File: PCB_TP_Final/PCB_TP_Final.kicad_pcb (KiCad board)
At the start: 2 copper layers, 5 parts, among them CN10 Conn_02x17_Odd_Even, CN7 Conn_02x10_Odd_Even, CN8 Conn_02x08_Odd_Even, CN9 Conn_02x15_Odd_Even, J1 Conn_01x09

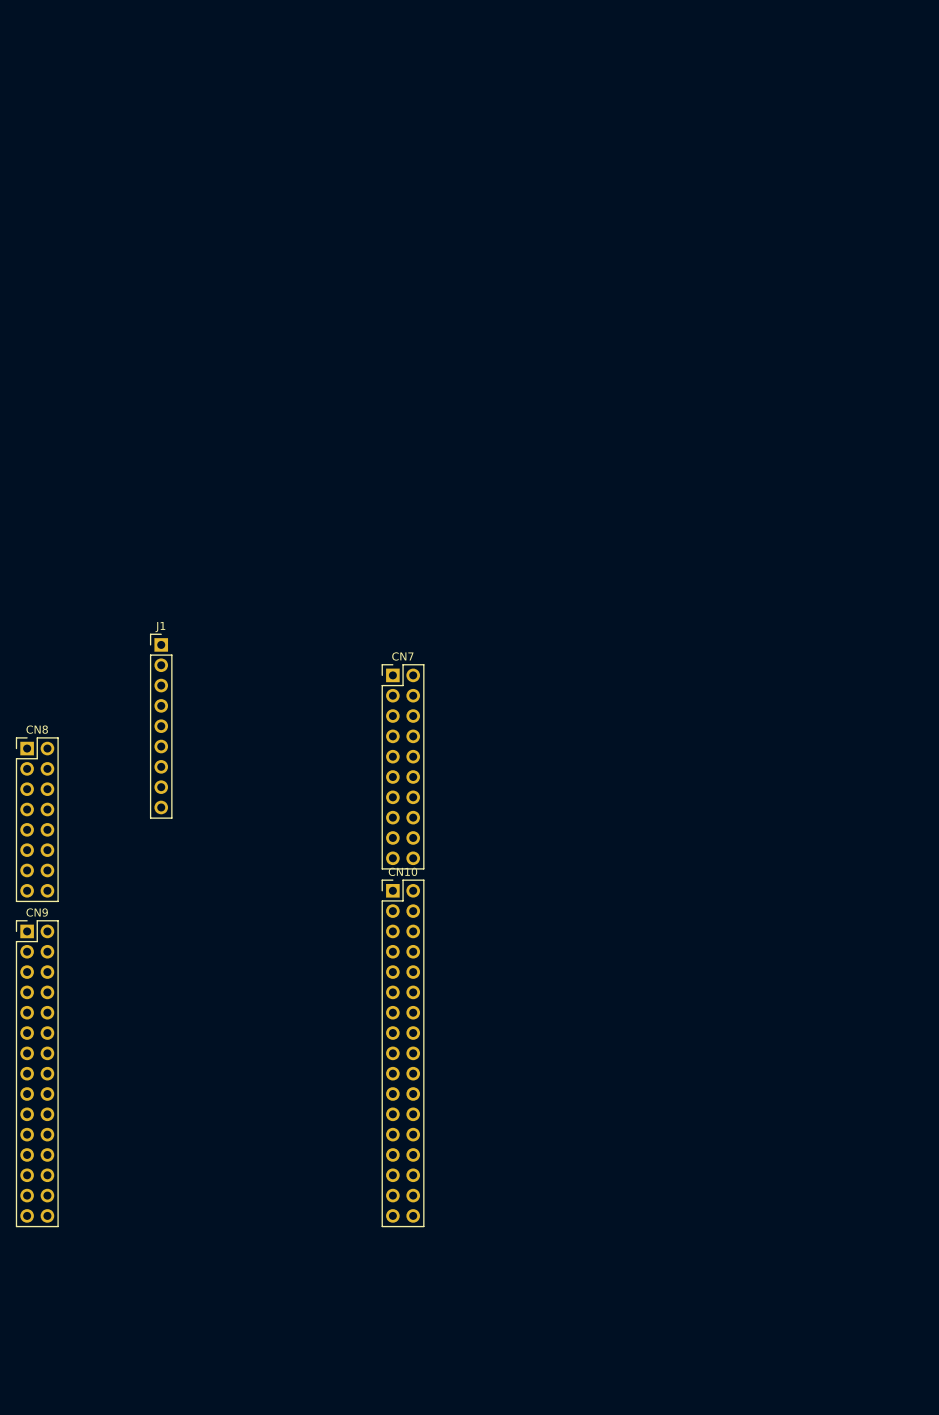
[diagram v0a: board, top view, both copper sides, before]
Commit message: Add footprint CODEC_AUDIO_WM8731
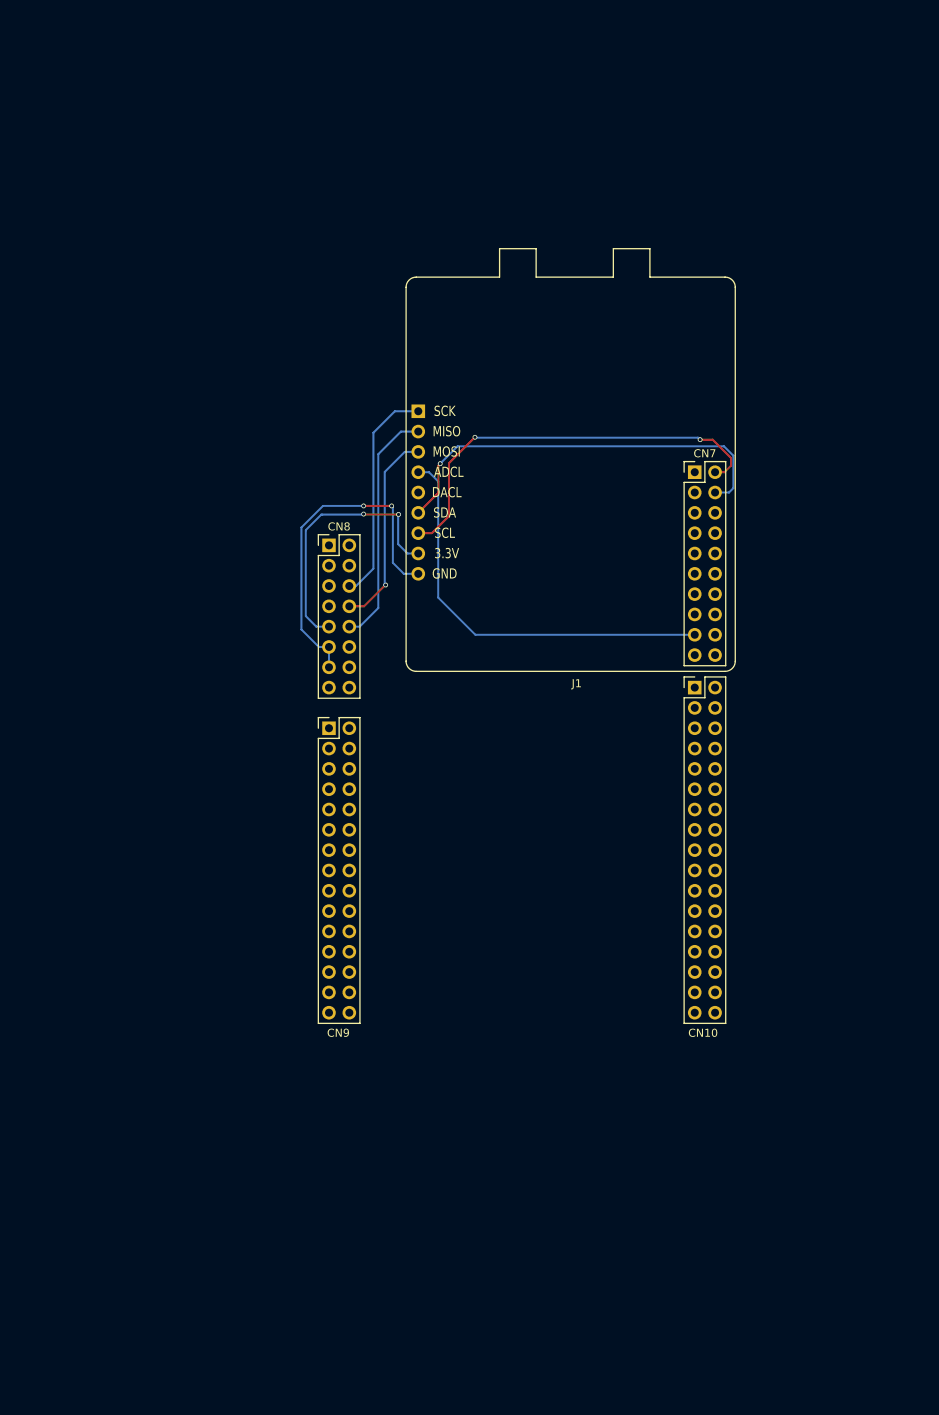
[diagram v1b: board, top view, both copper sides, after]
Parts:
- J1: footprint Connector_PinHeader_2.54mm:PinHeader_1x09_P2.54mm_Vertical -> CUSTOM_LIB:Audio_Codec_WM8731
- moved J1 55.0 mm to (132.2, 78.2)
- moved CN10 45.5 mm to (147.0, 101.6)
- moved CN8 45.5 mm to (101.2, 83.8)
- moved CN9 45.5 mm to (101.2, 106.7)
- moved CN7 45.5 mm to (147.0, 74.7)
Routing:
- net /AUDIO_CODEC/SCL: track 0.00 -> 52.3 mm, vias 0 -> 2
- net /AUDIO_CODEC/SDA: track 0.00 -> 51.9 mm, vias 0 -> 1
- net /AUDIO_CODEC/ADCL: track 0.00 -> 51.5 mm
- net GND: track 0.00 -> 43.0 mm, vias 0 -> 2
- net +3V3: track 0.00 -> 33.4 mm, vias 0 -> 2
- net /AUDIO_CODEC/MISO: track 0.00 -> 30.0 mm
- net /AUDIO_CODEC/SCK: track 0.00 -> 27.6 mm
- net /AUDIO_CODEC/MOSI: track 0.00 -> 25.1 mm, vias 0 -> 1

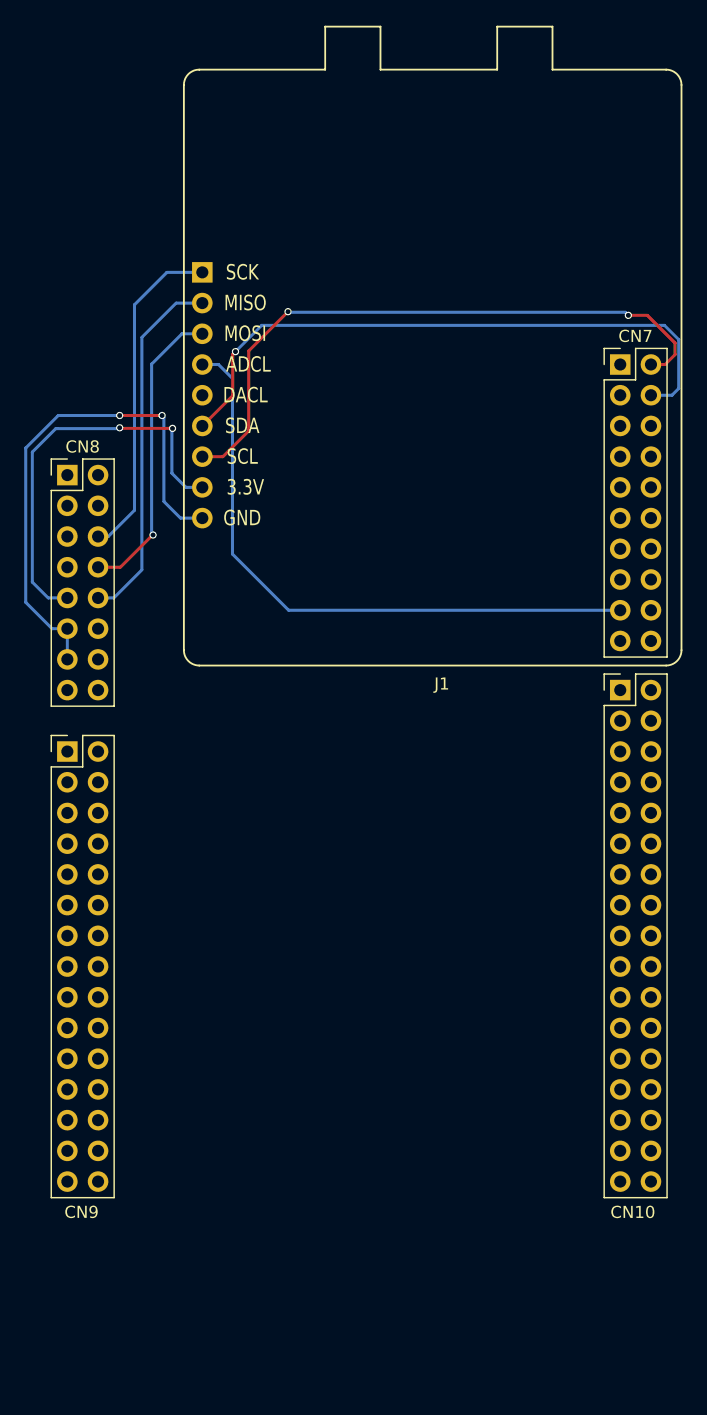
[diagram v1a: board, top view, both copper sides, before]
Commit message: Add 3D conections and NODEMCU ESP12
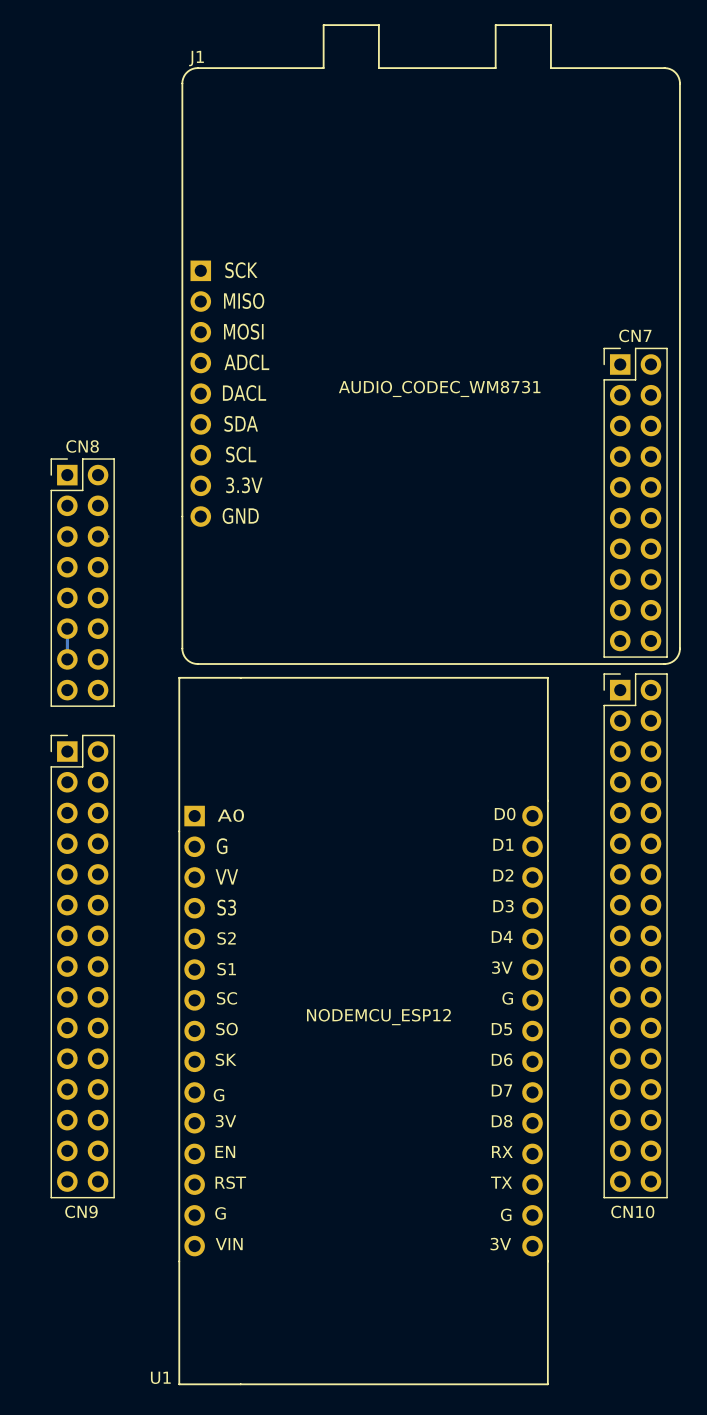
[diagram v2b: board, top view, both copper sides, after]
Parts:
- added U1: NODEMCU_ESP12, NODEMCU_ESP12:NODEMCU_ESP12, F.Cu at (127.0, 129.8)
- J1: footprint CUSTOM_LIB:Audio_Codec_WM8731 -> AUDIO_CODEC_WM8731:Audio_Codec_WM8731
- moved J1 0.18 mm to (132.1, 78.1)
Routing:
- net /AUDIO_CODEC/SCL: track 52.3 -> 0.00 mm, vias 2 -> 0
- net /AUDIO_CODEC/SDA: track 51.9 -> 0.00 mm, vias 1 -> 0
- net /AUDIO_CODEC/ADCL: track 51.5 -> 0.00 mm
- net GND: track 43.0 -> 2.54 mm, vias 2 -> 0
- net +3V3: track 33.4 -> 0.00 mm, vias 2 -> 0
- net /AUDIO_CODEC/MISO: track 30.0 -> 0.00 mm
- net /AUDIO_CODEC/SCK: track 27.6 -> 0.84 mm
- net /AUDIO_CODEC/MOSI: track 25.1 -> 0.00 mm, vias 1 -> 0

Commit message: Primera entrega (1.0) para revision
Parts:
- added M1: POWER_MB_V2, POWER_MB_V2:POWER_MB_V2, F.Cu at (124.5, 167.6)
- added R1: 3.3K, Resistors_SMD:R_1206, F.Cu at (120.0, 83.8)
- moved U1 2.29 mm to (127.0, 132.1)
- moved J1 0.90 mm to (131.4, 78.7)
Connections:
- CN10 pad 10: Net-(CN10-Pad10) -> /NODEMCU_ESP12/HMISO
- CN10 pad 26: Net-(CN10-Pad26) -> /NODEMCU_ESP12/HSCLK
- CN10 pad 28: Net-(CN10-Pad28) -> /NODEMCU_ESP12/HMOSI
- CN10 pad 6: Net-(CN10-Pad6) -> /NODEMCU_ESP12/HCS
- CN8 pad 9: +3V3 -> 3.3VB
- CN9 pad 12: Net-(CN9-Pad12) -> GND
- J1 pad 8: +3V3 -> 3.3VB
- U1 pad 16: Net-(U1-Pad16) -> +3V3
- U1 pad 20: Net-(U1-Pad20) -> /NODEMCU_ESP12/HCS
- U1 pad 21: Net-(U1-Pad21) -> /NODEMCU_ESP12/HMOSI
- U1 pad 22: Net-(U1-Pad22) -> /NODEMCU_ESP12/HMISO
- U1 pad 23: Net-(U1-Pad23) -> /NODEMCU_ESP12/HSCLK
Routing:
- net GND: track 2.54 -> 202.2 mm
- net /NODEMCU_ESP12/HMISO: track 0.00 -> 97.8 mm, vias 0 -> 1
- net /NODEMCU_ESP12/HCS: track 0.00 -> 93.5 mm, vias 0 -> 2
- net 3.3VB: track 0.00 -> 85.9 mm, vias 0 -> 1
- net /AUDIO_CODEC/SDA: track 0.00 -> 72.5 mm, vias 0 -> 2
- net /AUDIO_CODEC/ADCL: track 0.00 -> 51.3 mm
- net /AUDIO_CODEC/SCL: track 0.00 -> 49.5 mm, vias 0 -> 1
- net +3V3: track 0.00 -> 44.2 mm
- net /NODEMCU_ESP12/HSCLK: track 0.00 -> 40.6 mm
- net /AUDIO_CODEC/MOSI: track 0.00 -> 40.2 mm
- net /NODEMCU_ESP12/HMOSI: track 0.00 -> 32.9 mm
- net /AUDIO_CODEC/MISO: track 0.00 -> 28.8 mm, vias 0 -> 2
- net /AUDIO_CODEC/SCK: track 0.84 -> 27.9 mm
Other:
- board outline added: 61 x 127 mm
- net class Default: clearance 0.2 -> 0.4; trace_width 0.25 -> 0.6
- rule trace_clearance: 0.2 -> 0.4

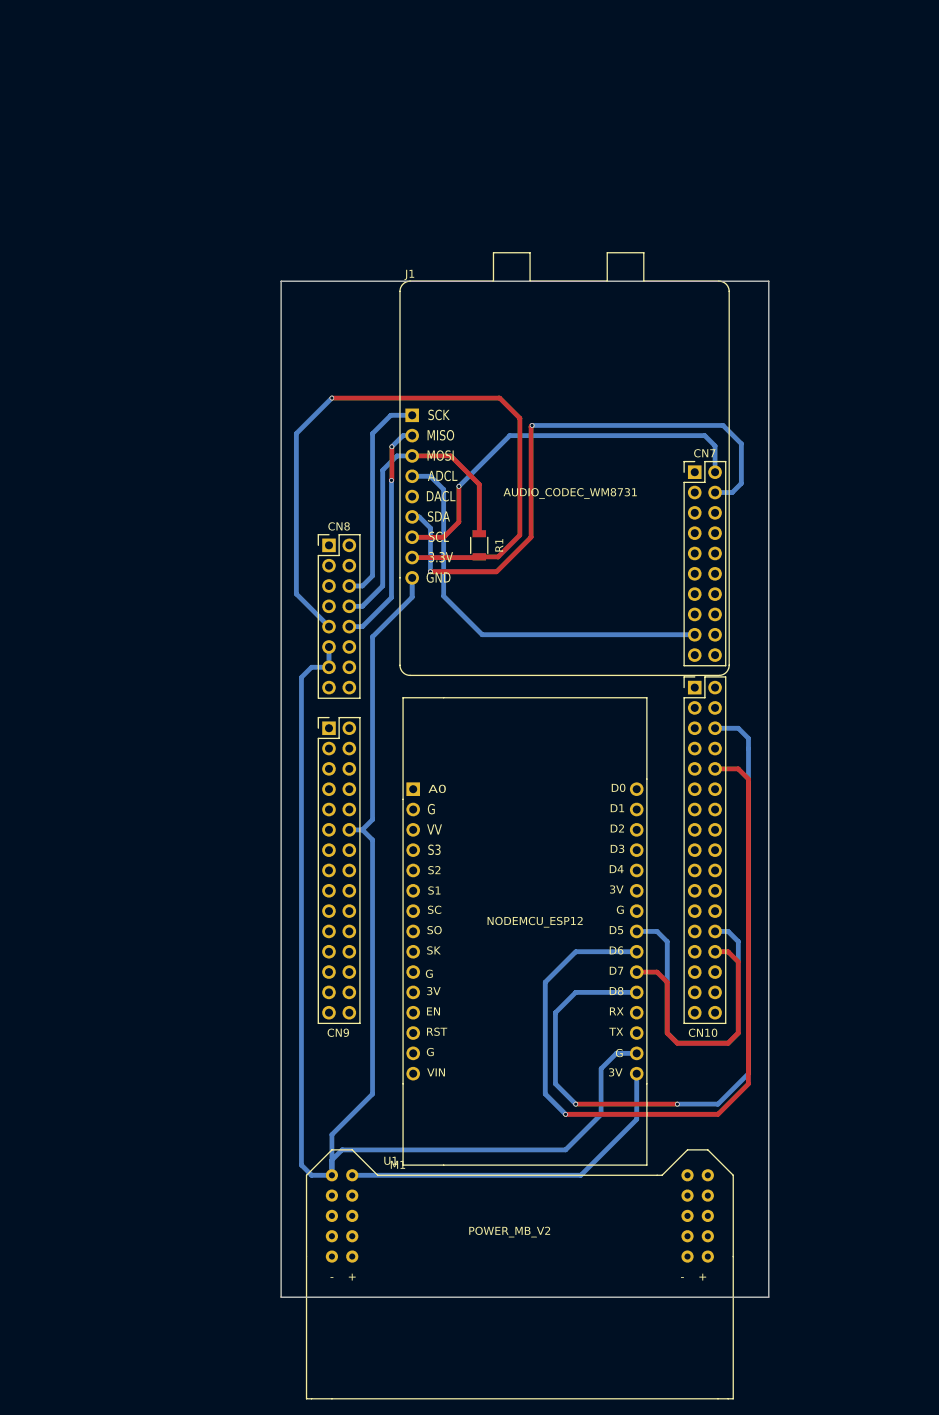
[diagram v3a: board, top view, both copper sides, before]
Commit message: Add size modify and mounting holes
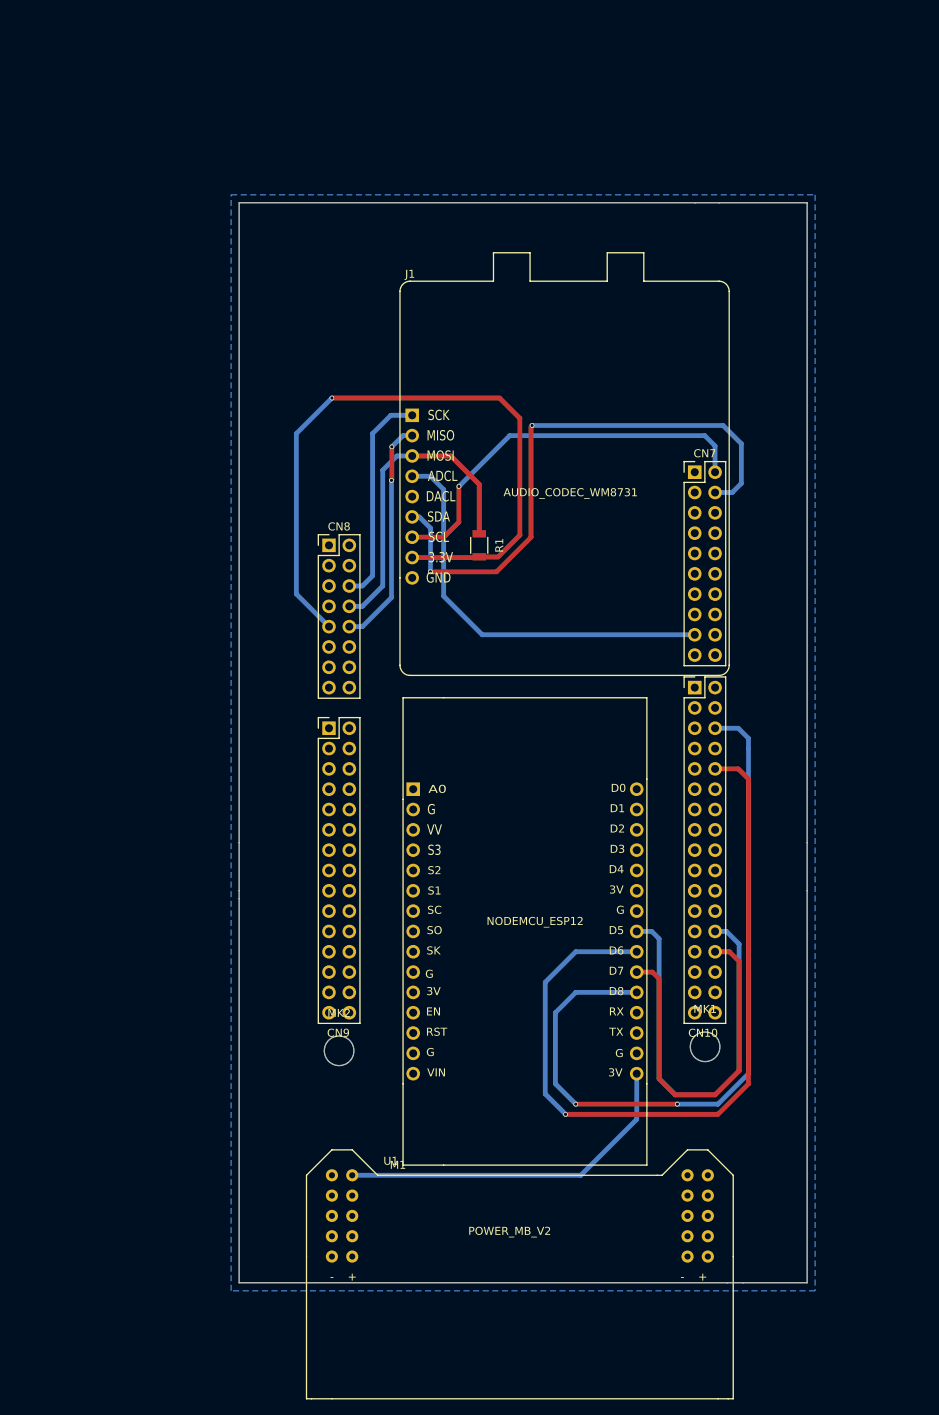
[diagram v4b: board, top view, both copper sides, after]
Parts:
- added MK1: Mounting_Hole, Mounting_Holes:MountingHole_3.7mm, F.Cu at (148.2, 146.5)
- added MK2: Mounting_Hole, Mounting_Holes:MountingHole_3.7mm, F.Cu at (102.5, 147.0)
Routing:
- net GND: track 202.2 -> 0.00 mm
- net /NODEMCU_ESP12/HMOSI: track 32.9 -> 44.9 mm
- net /NODEMCU_ESP12/HSCLK: track 40.6 -> 52.3 mm
- added copper zone on B.Cu, net GND
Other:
- board size 61 x 127 mm -> 71 x 135 mm

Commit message: Revisión 2.0 para evaluación
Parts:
- added C1: 0.1uF, Capacitors_SMD:C_0805_HandSoldering, F.Cu at (120.0, 40.5)
- added D1: LED, LEDs:LED_0805_HandSoldering, F.Cu at (121.0, 29.0)
- added F1: Fiducial, Fiducials:Fiducial_1mm_Dia_2.54mm_Outer_CopperBottom, F.Cu at (169.5, 153.0)
- added F2: Fiducial, Fiducials:Fiducial_1mm_Dia_2.54mm_Outer_CopperBottom, F.Cu at (128.5, 28.0)
- added F3: Fiducial, Fiducials:Fiducial_1mm_Dia_2.54mm_Outer_CopperTop, F.Cu at (108.5, 153.0)
- added F4: Fiducial, Fiducials:Fiducial_1mm_Dia_2.54mm_Outer_CopperTop, F.Cu at (169.5, 28.0)
- added R2: 330, Resistors_SMD:R_1206_HandSoldering, F.Cu at (116.5, 39.5)
- added R3: 100K, Resistors_SMD:R_1206_HandSoldering, F.Cu at (113.0, 39.5)
- added R4: 10K, Resistors_SMD:R_1206_HandSoldering, F.Cu at (109.5, 39.5)
- added SW1: SW_Push, Buttons_Switches_THT:SW_PUSH_6mm_h8mm, F.Cu at (109.5, 33.5)
- R1: footprint Resistors_SMD:R_1206 -> Resistors_SMD:R_1206_HandSoldering
- moved R1 23.2 mm to (133.5, 65.0)
- moved U1 22.5 mm to (140.5, 114.1)
- moved M1 22.5 mm to (138.0, 149.6)
- moved CN10 22.5 mm to (160.5, 83.6)
- moved CN7 22.5 mm to (160.5, 56.7)
- moved CN8 22.5 mm to (114.7, 65.8)
- moved CN9 22.5 mm to (114.7, 88.7)
- moved MK1 22.5 mm to (161.8, 128.5)
- moved MK2 22.5 mm to (116.0, 129.0)
- moved J1 22.5 mm to (144.9, 60.7)
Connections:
- CN9 pad 30: Net-(CN9-Pad30) -> /TalkButton/talk
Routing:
- net /TalkButton/talk: track 0.00 -> 110.6 mm, vias 0 -> 1
- net Net-(D1-Pad1): track 0.00 -> 27.9 mm
- net 3.3VB: track 85.9 -> 103.1 mm, vias 1 -> 2
- net Net-(D1-Pad2): track 0.00 -> 10.1 mm
- net GND: track 0.00 -> 3.03 mm, vias 0 -> 1
- net /NODEMCU_ESP12/HMOSI: track 44.9 -> 43.4 mm
- net /NODEMCU_ESP12/HSCLK: track 52.3 -> 50.7 mm
- net /AUDIO_CODEC/MOSI: track 40.2 -> 38.9 mm
- net /NODEMCU_ESP12/HMISO: track 97.8 -> 98.5 mm
- net /AUDIO_CODEC/SDA: track 72.5 -> 73.2 mm
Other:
- net class Default: via_dia 0.6 -> 1.2
- board text added: "Minimos (Mayer 100 mils): Grillas: 0.1270mm, 0.5mm, 0.6350mm, 2.54mm Via 1.2mm, 0.6mm: Margen: 0.4mm Pista: 0.6mm Dist. a borde: 0.6mm Terminación: HASL"
